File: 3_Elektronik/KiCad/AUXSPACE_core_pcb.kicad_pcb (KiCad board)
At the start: 4 copper layers, 60 x 60 mm, 77 parts, among them J1 Conn_02x10_Odd_Even, J2 Conn_02x10_Odd_Even, J3 Conn_02x10_Odd_Even, J4 Conn_02x10_Odd_Even, J5 PinHeader 2,54mm 3p, J6 693072010801, J7 629722000214, Q1 2N7002K, Q2 2N7002K, SW2 430481025816, U1 ADXL375BCCZ, U2 TPS7B8601QDDARQ1, U3 TCAN334, U4 ESP32-S3-WROOM-1, U5 LSM6DSO32XTR, U6 DPS310, U7 MLX90395xLW, U8 CH224A

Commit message: electronics: :sparkles: add BOOTSEL
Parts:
- added G***: LOGO, AUXSPACE:hampter, F.Cu at (140.5, 124.7)
- added G***: LOGO, AUXSPACE:stack_pwr, B.Cu at (142.8, 77.5)
- added G***: LOGO, AUXSPACE:mcu_meme, B.Cu at (175.0, 100.5)
- added G***: LOGO, AUXSPACE:stack_data, B.Cu at (142.0, 122.5)
- added R23: 390R, Resistor_SMD:R_0603_1608Metric, B.Cu at (154.0, 84.5)
- added SW3: 430481025816, AUXSPACE:SW_Wurth_WS-TASV_430481025816, B.Cu at (160.5, 86.5)
- moved Logo1 7.81 mm to (147.0, 123.0)
- moved D5 1.00 mm to (124.0, 115.5)
- moved R22 1.00 mm to (128.0, 115.5)
- moved D4 0.50 mm to (124.0, 112.0)
- moved R21 0.50 mm to (128.0, 112.0)
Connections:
- U4 pad 15: /Baseboard/I2C_SDA_top -> /Baseboard/SD_LED
- U4 pad 24: /Baseboard/Buzzer -> /Baseboard/I2C_SDA_top
- U4 pad 25: /Baseboard/STATE_LED -> /Baseboard/Buzzer
- U4 pad 33: /Baseboard/SD_LED -> /Baseboard/STATE_LED
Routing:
- net /Baseboard/I2C_SDA_top: track 25.8 -> 74.1 mm, vias 1 -> 3
- net /Baseboard/SD_LED: track 51.7 -> 33.7 mm
- net /Baseboard/STATE_LED: track 40.8 -> 53.8 mm
- net GND: track 130.3 -> 140.8 mm, vias 17 -> 20
- net /Baseboard/IO0: track 0.00 -> 10.4 mm
- net Net-(R23-Pad2): track 0.00 -> 9.18 mm
- net +3V3: track 88.1 -> 92.0 mm, vias 11 -> 12
- net /Baseboard/Buzzer: track 43.1 -> 45.2 mm
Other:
- board text added: "BOOTSEL"
- board text added: "GND"
- board text added: "RESET"
- board text added: "RXD"
- board text added: "SD"
- board text added: "State"
- board text added: "TXD"
- board text added: "UART"

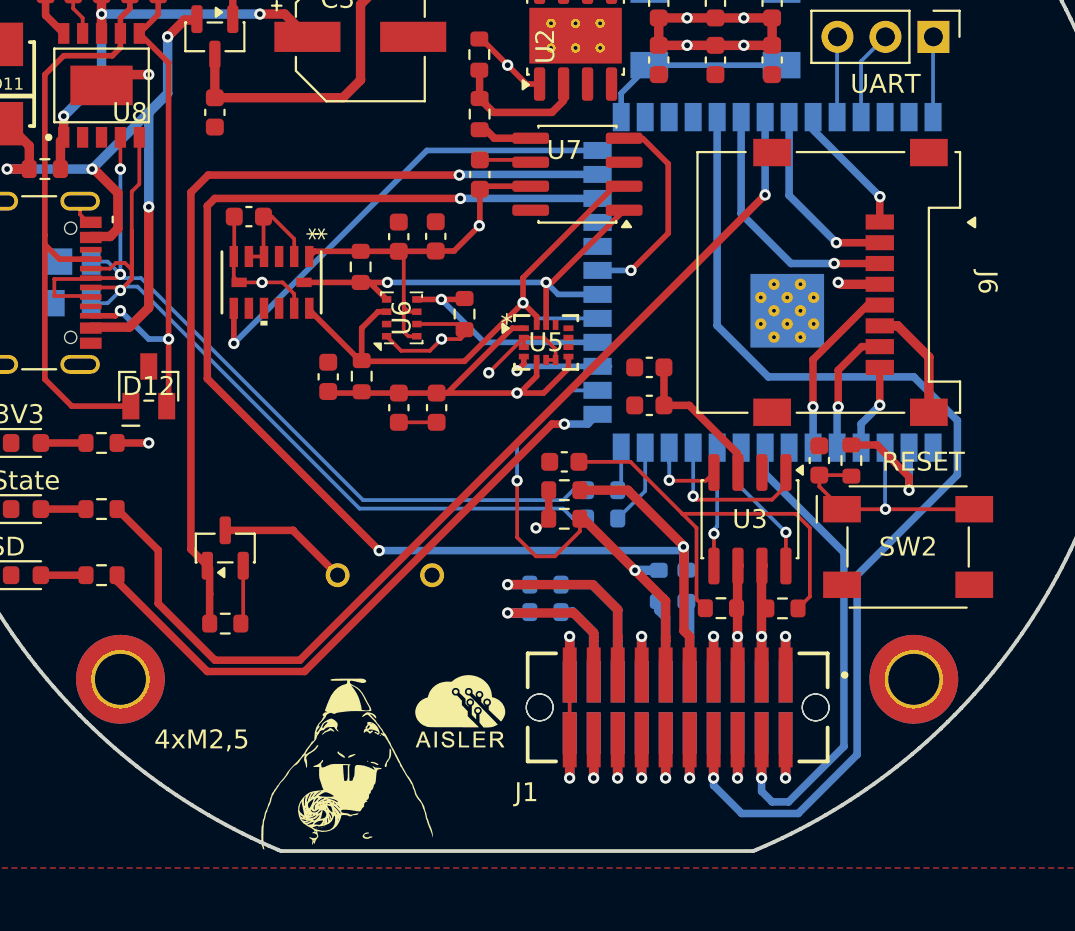
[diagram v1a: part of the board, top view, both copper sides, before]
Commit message: added UART top/bottom and Liftoff cnonection to µC
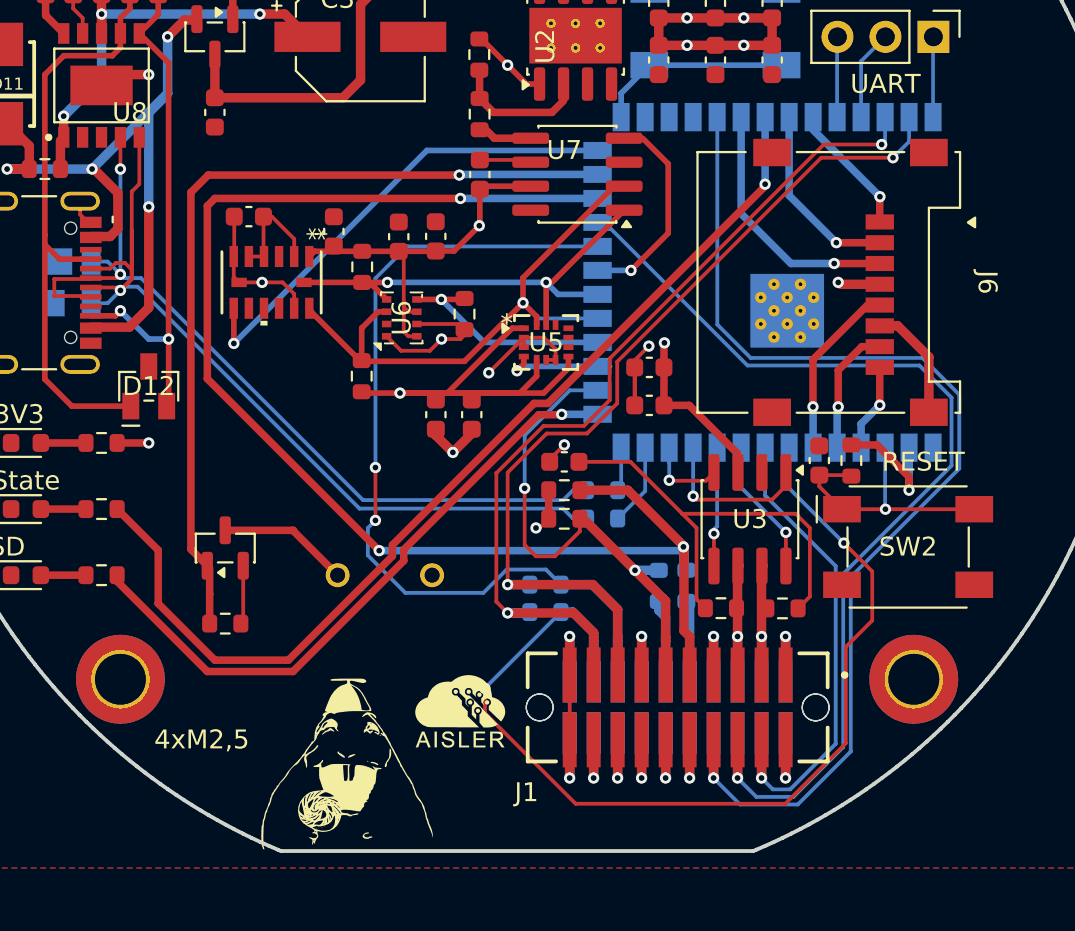
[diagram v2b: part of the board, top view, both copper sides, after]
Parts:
- C19: value 1uF -> 1µF
- C23: value 1.0uF -> 1µF
- C5, C6: value 100n -> 100nF
- moved C22 7.71 mm to (140.3, 97.3)
- moved C18 1.99 mm to (145.7, 107.0)
- moved C12 1.90 mm to (147.6, 107.0)
- moved R9 0.08 mm to (141.8, 99.2)
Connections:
- U4 pad 22: unconnected-(U4-IO14-Pad22) -> /Baseboard/UART_TX_bot
- U4 pad 23: unconnected-(U4-IO21-Pad23) -> /Baseboard/LIFTOFF
- U4 pad 38: unconnected-(U4-IO2-Pad38) -> /Baseboard/UART_RX_top
- U4 pad 39: unconnected-(U4-IO1-Pad39) -> /Baseboard/UART_TX_top
- U4 pad 7: unconnected-(U4-IO7-Pad7) -> /Baseboard/UART_RX_bot
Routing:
- net /Baseboard/LIFTOFF: track 4.40 -> 55.0 mm
- net /Baseboard/UART_RX_bot: track 5.60 -> 53.1 mm, vias 0 -> 2
- net /Baseboard/UART_TX_bot: track 8.18 -> 47.4 mm, vias 0 -> 2
- net /Baseboard/UART_RX_top: track 8.50 -> 46.6 mm, vias 1 -> 2
- net /Baseboard/UART_TX_top: track 11.0 -> 48.1 mm, vias 1 -> 2
- net GND: track 140.8 -> 148.7 mm, vias 20 -> 23
- net +3V3: track 92.0 -> 96.9 mm, vias 12 -> 13
- net /Baseboard/ARM: track 28.8 -> 26.8 mm

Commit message: improved Layout
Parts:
- C13, C14, C15, C16, C17, R15: moved to B.Cu
- moved C15 29.4 mm to (171.4, 113.5), turned to 0 degrees
- moved C17 28.9 mm to (171.4, 112.0), turned to 0 degrees
- moved C14 28.8 mm to (171.4, 110.5), turned to 0 degrees
- moved C4 17.1 mm to (149.4, 83.7)
- moved C10 14.9 mm to (157.6, 102.8), turned to 180 degrees
- moved C9 14.3 mm to (157.6, 101.3), turned to 180 degrees
- moved C16 12.1 mm to (162.4, 116.5), turned to -90 degrees
- moved C11 8.05 mm to (149.6, 86.7), turned to -90 degrees
- moved C13 2.46 mm to (167.6, 111.3), turned to -90 degrees
- moved R15 2.34 mm to (169.1, 111.3), turned to 90 degrees
- moved C7 0.78 mm to (157.6, 105.0)
- moved C8 0.60 mm to (157.6, 106.5)
- moved C5 0.53 mm to (144.1, 97.2)
- moved C6 0.37 mm to (145.6, 97.2)
- moved C22 0.10 mm to (140.3, 97.2)
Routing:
- net GND: track 148.7 -> 223.5 mm, vias 23 -> 39
- net Net-(C16-Pad2): track 23.7 -> 7.99 mm, vias 0 -> 2
- net /Baseboard/SD_LED: track 34.1 -> 32.3 mm
- net +3V3: track 96.9 -> 95.6 mm, vias 13 -> 8
- net /Baseboard/UART_RX_top: track 46.6 -> 47.8 mm
- net /Baseboard/UART_TX_top: track 48.1 -> 49.3 mm
- net Net-(U8-VBUS): track 23.9 -> 24.5 mm
- removed copper zone on B.Cu, net GND
- removed copper zone on F.Cu, net GND
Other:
- board text added: "X+"
- board text added: "Y+"
- board text added: "Z+"
